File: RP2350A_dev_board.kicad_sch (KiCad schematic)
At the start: 45 parts, among them J1 Debug Headers, J2 USB_C_Female_USB2.0_16P, J3 I2C Headers, SW1 Button, SW2 Button, U1 USBLC6-2SC6, U2 SPX3819M5-L-3-3, U3 RP2350A, U4 W25Q128JVS, Y1 12MHz Crystal GND2,4

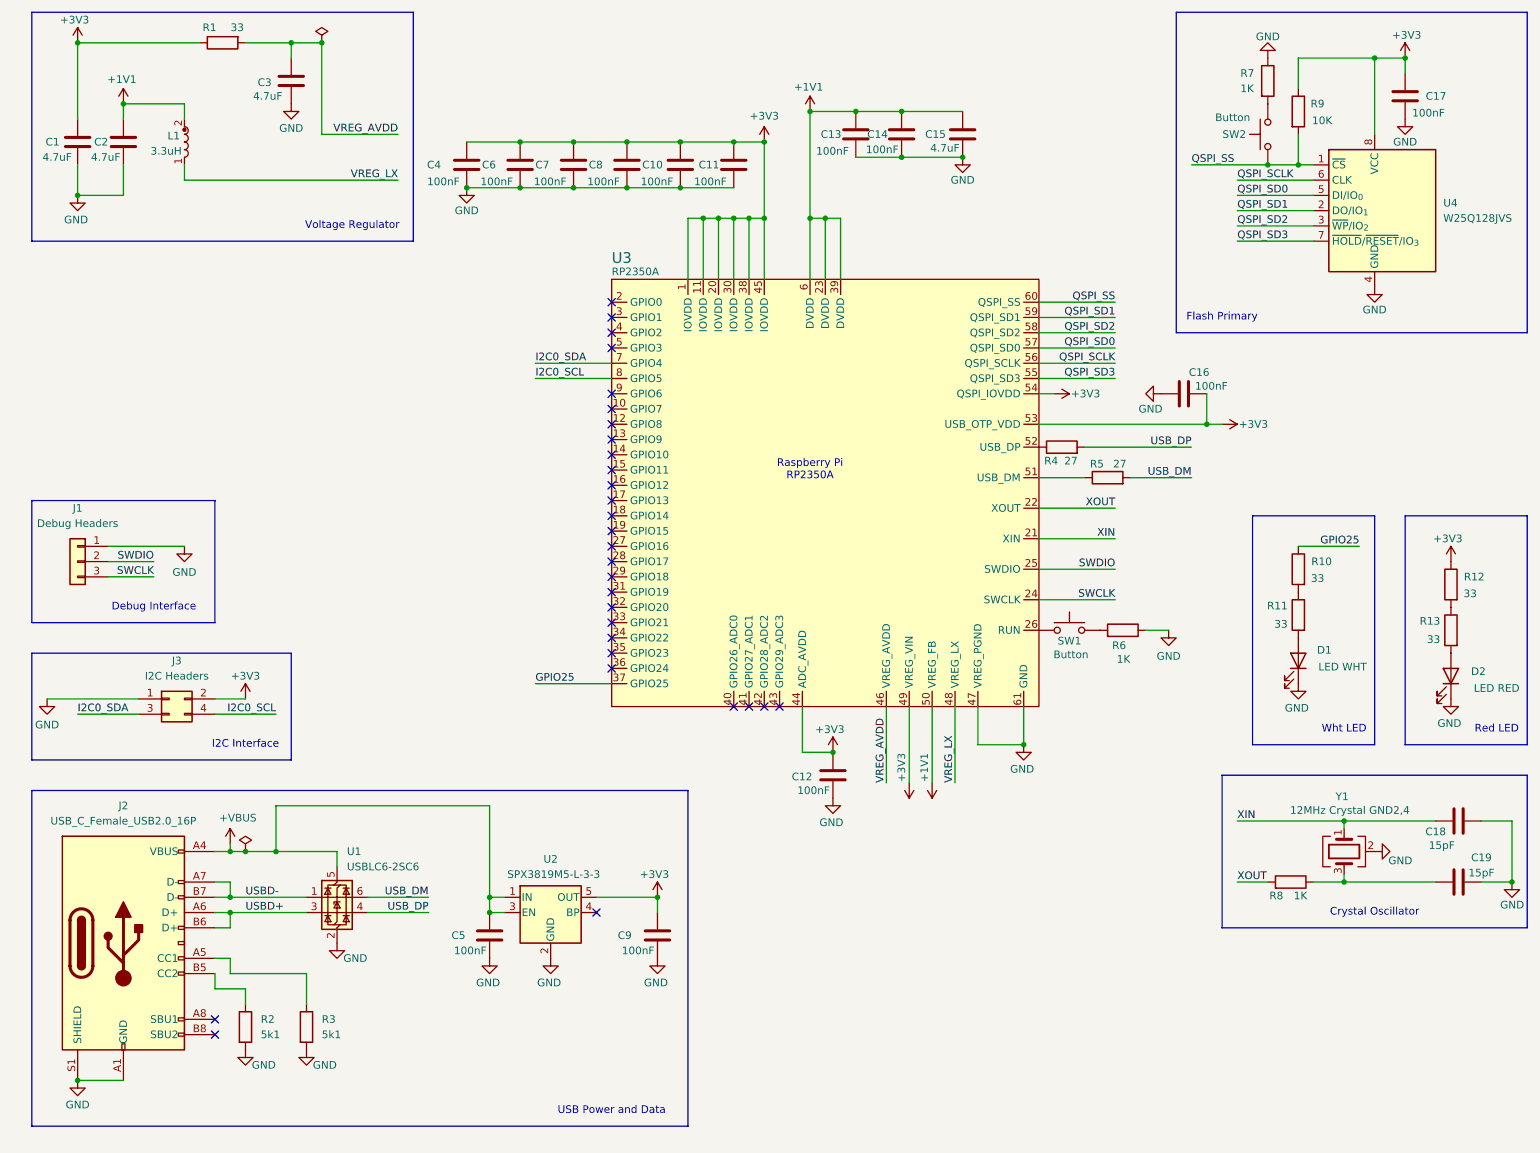
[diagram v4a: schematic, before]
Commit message: Reorganized for readability.
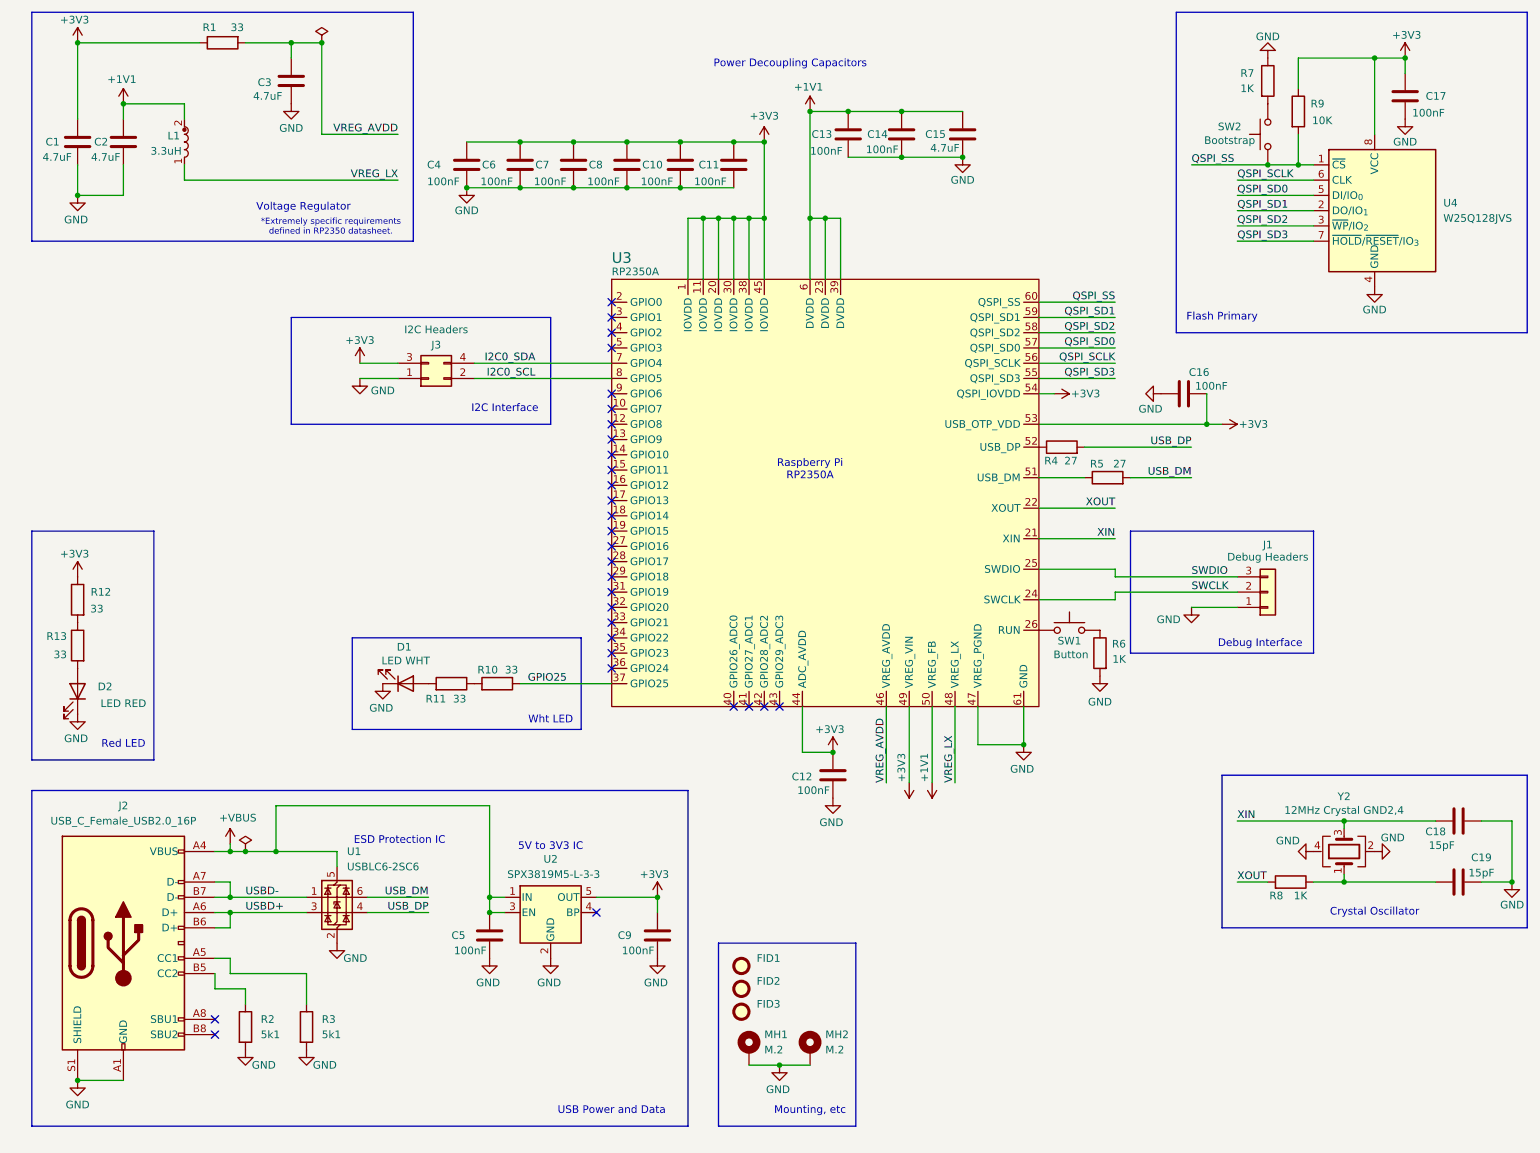
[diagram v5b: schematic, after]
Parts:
- removed Y1: 12MHz Crystal GND2,4, oscillators:ABM8-272-T3, symbol Device:Crystal_GND24
- added FID1, FID2, FID3: ~, Fiducial:Fiducial_1mm_Mask2mm, symbol Mechanical:Fiducial
- added MH1, MH2: M.2, MountingHole:MountingHole_2.2mm_M2_Pad_Via, symbol Mechanical:MountingHole_Pad
- added Y2: 12MHz Crystal GND2,4, oscillators:ABM8-272-T3, symbol custom:Crystal_GND24_custom
- SW2: value Button -> Bootstrap
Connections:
- net +3V3: now also J3.3 (Pin_3); no longer J3.2 (Pin_2)
- net GND: now also R6.2, MH1.1, MH2.1, Y2.2 (G), Y2.4 (G); no longer R6.1
- net I2C0_SCL: now also J3.2 (Pin_2); no longer J3.4 (Pin_4)
- net I2C0_SDA: now also J3.4 (Pin_4); no longer J3.3 (Pin_3)
- net SWCLK: now also J1.2 (Pin_2); no longer J1.3 (Pin_3)
- net SWDIO: now also J1.3 (Pin_3); no longer J1.2 (Pin_2)
- net XIN: now also Y2.3
- net at SW1.2: now also R6.1; no longer R6.2
- net at C19.2, R8.1: now also Y2.1
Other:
- note added: "*Extremely specific requirements defined in RP2350 datasheet."
- note added: "5V to 3V3 IC"
- note added: "ESD Protection IC"
- note added: "Mounting, etc"
- note added: "Power Decoupling Capacitors"
- company: Nathaniel Graves -> N####### G####
- moved on the sheet: C13, D1, D2, J1, J3, R10, R11, R12, R13, R6

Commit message: Reorganized again.
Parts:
- U4: symbol Memory_Flash:W25Q128JVS -> custom:W25Q128JVS_custom
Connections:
- net QSPI_SS: now also SW2.2; no longer SW2.1
- net at R7.2: now also SW2.1; no longer SW2.2
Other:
- note added: "Flash Chip"
- moved on the sheet: C16, C17, R7, R9, SW2, U4

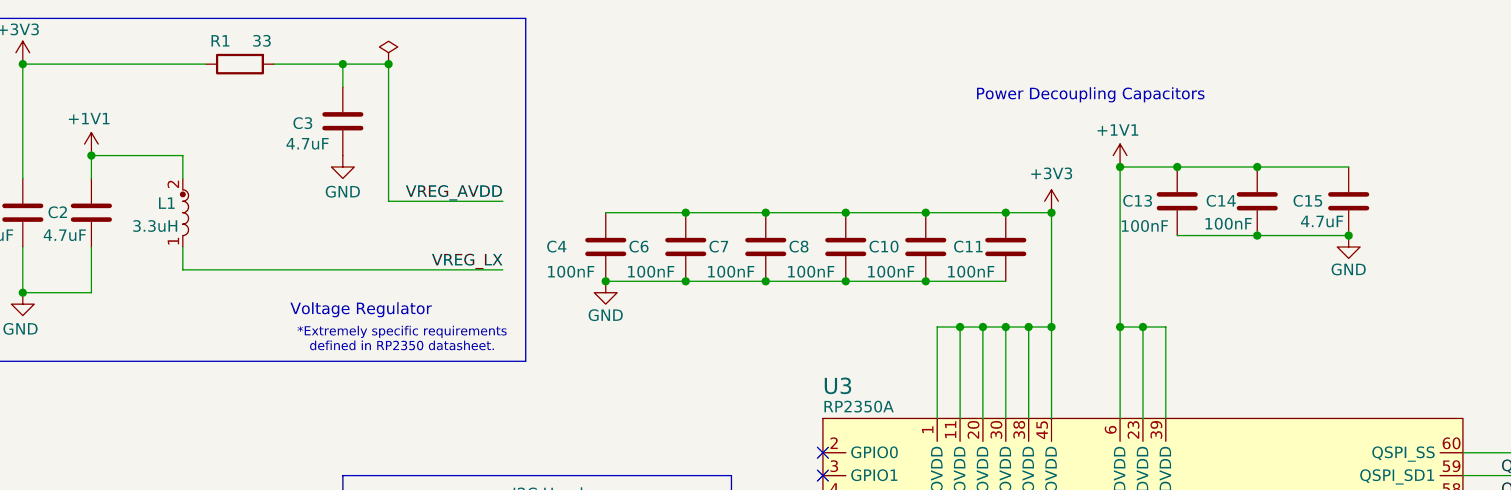
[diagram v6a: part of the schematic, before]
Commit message: Began PCB Layout. reorganized DVDD decoupling capacitors for readability. Fixed L1 inductor footprint, Y2 Crystal footprint.
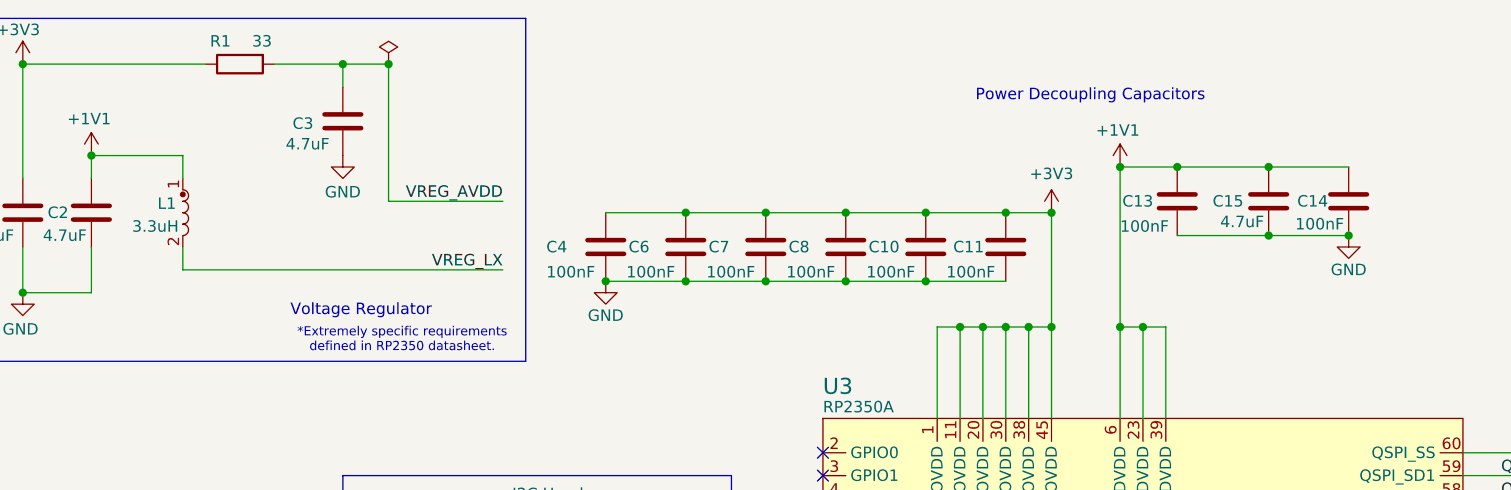
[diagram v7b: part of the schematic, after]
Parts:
- L1: footprint inductors:AOTA-B201610S3R3-101-T -> custom:AOTA-B201610S3R3-101-T_custom
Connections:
- net +1V1: now also L1.1; no longer L1.2
- net VREG_LX: now also L1.2; no longer L1.1
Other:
- moved on the sheet: C14, C15
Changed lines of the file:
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@@
 	)
 	(junction
+		(at 161.29 39.37)
+		(diameter 0)
+		(color 0 0 0 0)
+	)
+	(junction
 		(at 58.42 20.32)
 		(diameter 0)
@@
 	)
 	(junction
-		(at 170.18 39.37)
-		(diameter 0)
-		(color 0 0 0 0)
-	)
-	(junction
 		(at 55.88 154.94)
 		(diameter 0)
@@
 	)
 	(junction
-		(at 160.02 31.75)
+		(at 180.34 137.16)
 		(diameter 0)
 		(color 0 0 0 0)
 	)
 	(junction
-		(at 180.34 137.16)
+		(at 129.54 49.53)
 		(diameter 0)
 		(color 0 0 0 0)
 	)
 	(junction
-		(at 129.54 49.53)
+		(at 161.29 31.75)
 		(diameter 0)
 		(color 0 0 0 0)
@@
 	)
 	(junction
+		(at 170.18 39.37)
+		(diameter 0)
+		(color 0 0 0 0)
+	)
+	(junction
 		(at 144.78 49.53)
 		(diameter 0)
@@
 	)
 	(junction
-		(at 160.02 39.37)
-		(diameter 0)
-		(color 0 0 0 0)
-	)
-	(junction
 		(at 123.19 36.83)
 		(diameter 0)
@@
 	(wire
 		(pts
-			(xy 151.13 39.37) (xy 160.02 39.37)
+			(xy 151.13 39.37) (xy 161.29 39.37)
 		)
 		(stroke
@@
 	(wire
 		(pts
+			(xy 161.29 39.37) (xy 170.18 39.37)
+		)
+		(stroke
+			(width 0)
+			(type default)
+		)
+	)
+	(wire
+		(pts
 			(xy 182.88 66.04) (xy 195.58 66.04)
 		)
@@
 	(wire
 		(pts
-			(xy 87.63 36.83) (xy 96.52 36.83)
+			(xy 161.29 31.75) (xy 170.18 31.75)
 		)
 		(stroke
@@
 	(wire
 		(pts
-			(xy 45.72 167.64) (xy 48.26 167.64)
+			(xy 87.63 36.83) (xy 96.52 36.83)
 		)
 		(stroke
@@
 	(wire
 		(pts
-			(xy 160.02 31.75) (xy 170.18 31.75)
+			(xy 45.72 167.64) (xy 48.26 167.64)
 		)
 		(stroke
@@
 	(wire
 		(pts
-			(xy 151.13 31.75) (xy 160.02 31.75)
+			(xy 151.13 31.75) (xy 161.29 31.75)
 		)
 		(stroke
@@
 	(wire
 		(pts
-			(xy 160.02 39.37) (xy 170.18 39.37)
-		)
-		(stroke
-			(width 0)
-			(type default)
-		)
-	)
-	(wire
-		(pts
 			(xy 144.78 49.53) (xy 144.78 59.69)
 		)
@@
 	(symbol
 		(lib_id "Device:C")
-		(at 160.02 35.56 0)
+		(at 170.18 35.56 0)
 		(mirror y)
 		(unit 1)
@@
 		(dnp no)
 		(property "Reference" "C14"
-			(at 157.734 35.56 0)
+			(at 167.894 35.56 0)
 			(effects
 				(font
@@
 		)
 		(property "Value" "100nF"
-			(at 159.512 38.1 0)
+			(at 169.672 38.1 0)
 			(effects
 				(font
@@
 		)
 		(property "Footprint" "Capacitor_SMD:C_0603_1608Metric"
-			(at 159.0548 39.37 0)
+			(at 169.2148 39.37 0)
 			(effects
 				(font
@@
 		)
 		(property "Datasheet" "https://jlcpcb.com/api/file/downloadByFileSystemAccessId/8667086713681608704"
-			(at 160.02 35.56 0)
+			(at 170.18 35.56 0)
 			(effects
 				(font
@@
 		)
 		(property "Description" "100nF 50V X7R ±10% 0603 Multilayer Ceramic Unpolarized Capacitors"
-			(at 160.02 35.56 0)
+			(at 170.18 35.56 0)
 			(effects
 				(font
@@
 		)
 		(property "Manufacturer" "YAGEO"
-			(at 160.02 35.56 0)
+			(at 170.18 35.56 0)
 			(effects
 				(font
@@
 		)
 		(property "Manufacturer Part Number" "CC0603KRX7R9BB104"
-			(at 160.02 35.56 0)
+			(at 170.18 35.56 0)
 			(effects
 				(font
@@
 		)
 		(property "Distributor Link 1" "https://www.mouser.com/ProductDetail/YAGEO/CC0603KRX7R9BB104?qs=vTakOoo5QyLvVCYM2ge8LQ%3D%3D"
-			(at 160.02 35.56 0)
+			(at 170.18 35.56 0)
 			(effects
 				(font
@@
 		)
 		(property "Distributor Link 2" "https://www.digikey.com/en/products/detail/yageo/CC0603KRX7R9BB104/2103082?s=N4IgTCBcDaIMJwAwDZEGYDSAlAGgdiwE4AhYgRkQBYQBdAXyA"
-			(at 160.02 35.56 0)
+			(at 170.18 35.56 0)
 			(effects
 				(font
@@
 		)
 		(property "LCSC Part Number" "C14663"
-			(at 160.02 35.56 0)
+			(at 170.18 35.56 0)
 			(effects
 				(font
@@
 	(symbol
 		(lib_id "Device:C")
-		(at 170.18 35.56 0)
+		(at 161.29 35.56 0)
 		(mirror y)
 		(unit 1)
@@
 		(dnp no)
 		(property "Reference" "C15"
-			(at 167.386 35.56 0)
+			(at 158.496 35.56 0)
 			(effects
 				(font
@@
 		)
 		(property "Value" "4.7uF"
-			(at 169.672 37.846 0)
+			(at 160.782 37.846 0)
 			(effects
 				(font
@@
 		)
 		(property "Footprint" "Capacitor_SMD:C_0603_1608Metric"
-			(at 169.2148 39.37 0)
+			(at 160.3248 39.37 0)
 			(effects
 				(font
@@
 		)
 		(property "Datasheet" "https://www.lcsc.com/datasheet/C19666.pdf"
-			(at 170.18 35.56 0)
+			(at 161.29 35.56 0)
 			(effects
 				(font
@@
 		)
 		(property "Description" "Capacitor, 4.7uF ±10% 16V Ceramic X5R 0603"
-			(at 170.18 35.56 0)
+			(at 161.29 35.56 0)
 			(effects
 				(font
@@
 		)
 		(property "Manufacturer" "Samsung Electro-Mechanics"
-			(at 170.18 35.56 0)
+			(at 161.29 35.56 0)
 			(effects
 				(font
@@
 		)
 		(property "Manufacturer Part Number" "CL10A475KO8NNNC"
-			(at 170.18 35.56 0)
+			(at 161.29 35.56 0)
 			(effects
 				(font
@@
 		)
 		(property "Distributor Link 1" "https://www.mouser.com/ProductDetail/Samsung-Electro-Mechanics/CL10A475KO8NNNC?qs=X6jEic%2FHinAbIjmLnFfqqQ%3D%3D"
-			(at 170.18 35.56 0)
+			(at 161.29 35.56 0)
 			(effects
 				(font
@@
 		)
 		(property "Distributor Link 2" "https://www.digikey.com/en/products/detail/samsung-electro-mechanics/CL10A475KO8NNNC/3887442?s=N4IgTCBcDaIMIBkCMAGAggFgOwFYDSA8gBwByZcABCALoC%2BQA"
-			(at 170.18 35.56 0)
+			(at 161.29 35.56 0)
 			(effects
 				(font
@@
 		)
 		(property "LCSC Part Number" "C19666"
-			(at 170.18 35.56 0)
+			(at 161.29 35.56 0)
 			(effects
 				(font
@@
 			)
 		)
-		(property "Footprint" "inductors:AOTA-B201610S3R3-101-T"
+		(property "Footprint" "custom:AOTA-B201610S3R3-101-T_custom"
 			(at 39.116 30.226 0)
 			(effects

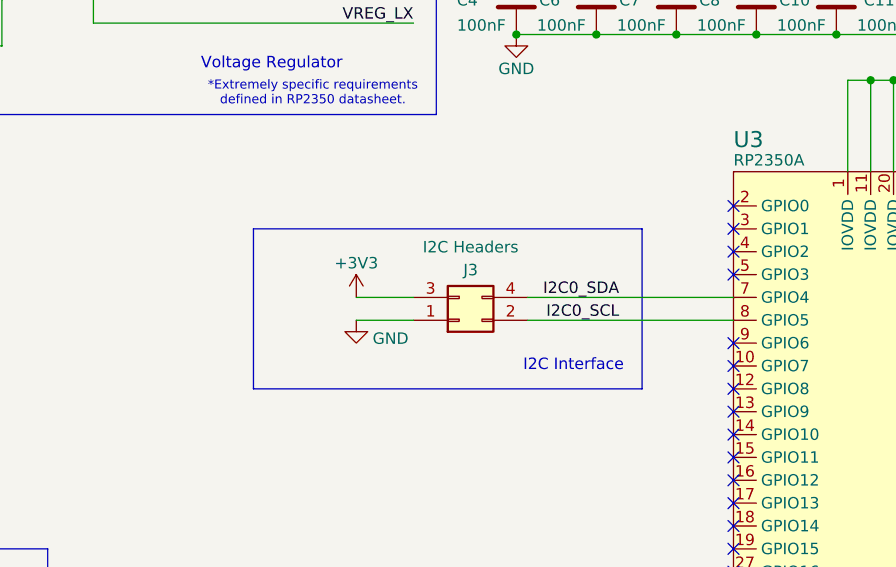
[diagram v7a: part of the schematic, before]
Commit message: Finished rough layout. Incorporated 5.1K pull-up resistors for I2C lines.
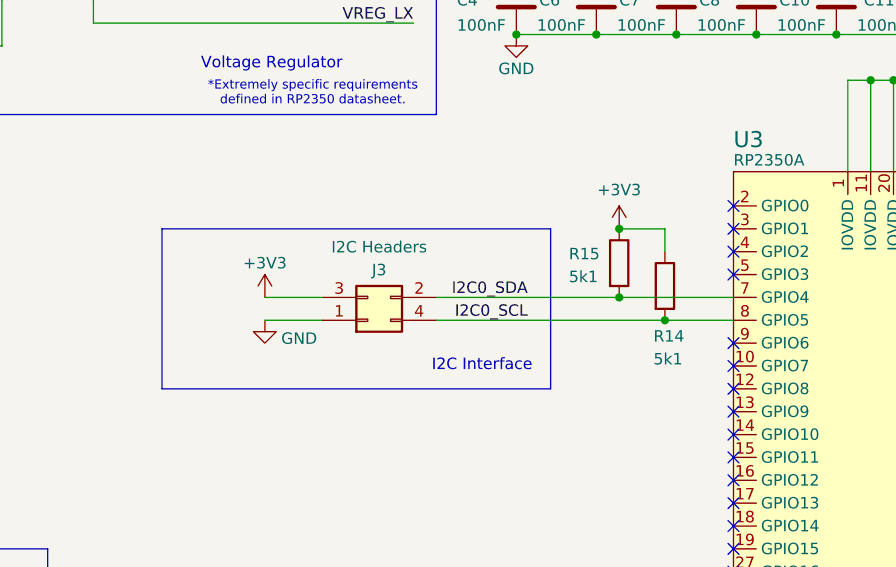
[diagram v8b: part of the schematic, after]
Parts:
- added R14, R15: 5k1, Resistor_SMD:R_0603_1608Metric, symbol Device:R
- J3: symbol Connector_Generic:Conn_02x02_Odd_Even -> custom:Conn_02x02_Odd_Even_custom
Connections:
- net +3V3: now also R14.1, R15.1
- net I2C0_SCL: now also J3.4 (Pin_2), R14.2; no longer J3.2 (Pin_2)
- net I2C0_SDA: now also J3.2 (Pin_4), R15.2; no longer J3.4 (Pin_4)
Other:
- moved on the sheet: J3
